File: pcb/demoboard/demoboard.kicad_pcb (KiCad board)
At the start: 2 copper layers, 68.6 x 48.3 mm, 34 parts, among them J1 BTN, J10 Conn_01x15, J11 Servo2, J12 TEMP, J13 MOT_A, J14 MOT_B, J15 CAP_T, J16 ANALOG, J17 7SEG1, J18 7SEG2, J19 STEPPER1, J2 BAT, J20 STEPPER2, J21 BITS, J22 OLED, J23 Servo3, J24 LIGHT, J3 Conn_01x15, J4 Conn_01x04, J5 Conn_01x15, J6 WSLED, J8 Conn_01x15, J9 Servo1, U2 L293D, U3 PCF8574, U4 ULN2803A

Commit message: PCB 0.1
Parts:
- removed J15: CAP_T, Connector_PinSocket_2.54mm:PinSocket_1x04_P2.54mm_Vertical
- removed J21: BITS, Connector_PinSocket_2.54mm:PinSocket_1x10_P2.54mm_Vertical
- removed REF** (x2): TestPoint_Pad_1.5x1.5mm, TestPoint:TestPoint_Pad_1.5x1.5mm
- removed U3: PCF8574, Package_DIP:DIP-16_W7.62mm
- added R5: 4K7, Resistor_THT:R_Axial_DIN0207_L6.3mm_D2.5mm_P10.16mm_Horizontal, F.Cu at (83.8, 99.7)
- added U1: 74HC595, Package_DIP:DIP-16_W7.62mm, F.Cu at (96.5, 115.6)
- J1: footprint Connector_PinSocket_2.54mm:PinSocket_1x03_P2.54mm_Vertical -> Connector_PinSocket_2.54mm:PinSocket_1x03_P2.54mm_Horizontal
- J10, J3, J5, J8: footprint Connector_PinSocket_2.54mm:PinSocket_1x15_P2.54mm_Vertical -> plain:PlainPinSocket_1x15_P2.54mm_Vertical
- J11, J23, J6, J9: footprint Connector_PinHeader_2.54mm:PinHeader_1x03_P2.54mm_Vertical -> plain:PlainPinHeader_1x03_P2.54mm_Vertical
- J12, RV1: footprint Connector_PinSocket_2.54mm:PinSocket_1x03_P2.54mm_Vertical -> plain:PlainPinSocket_1x03_P2.54mm_Vertical
- J17, J18: footprint Connector_PinSocket_2.54mm:PinSocket_1x05_P2.54mm_Vertical -> plain:PlainPinSocket_1x05_P2.54mm_Vertical
- J22: footprint Connector_PinSocket_2.54mm:PinSocket_1x04_P2.54mm_Vertical -> plain:PlainPinSocket_1x04_P2.54mm_Vertical
- J24: value LIGHT -> RV2; footprint Connector_PinSocket_2.54mm:PinSocket_1x02_P2.54mm_Vertical -> plain:PlainPinSocket_1x02_P2.54mm_Vertical
- R2, R3: value 4K7 -> 220R; footprint Resistor_THT:R_Axial_DIN0207_L6.3mm_D2.5mm_P10.16mm_Horizontal -> Resistor_THT:R_Axial_DIN0207_L6.3mm_D2.5mm_P2.54mm_Vertical
- moved R3 57.7 mm to (118.7, 90.8), turned to 180 degrees
- moved J6 49.5 mm to (120.7, 76.2), turned to 0 degrees
- moved J14 47.6 mm to (69.3, 77.5)
- moved R2 46.1 mm to (118.7, 87.0), turned to 180 degrees
- moved J1 45.7 mm to (106.7, 78.1), turned to 270 degrees
- moved J19 33.2 mm to (129.5, 118.1), turned to 180 degrees
- moved J9 22.2 mm to (127.6, 85.1), turned to 270 degrees
- moved J16 18.9 mm to (110.5, 95.2), turned to 180 degrees
- moved R1 17.6 mm to (67.3, 111.8)
- moved J18 16.9 mm to (110.5, 116.8), turned to 180 degrees
- moved U4 16.1 mm to (121.9, 116.8), turned to 180 degrees
- moved J24 13.9 mm to (71.1, 89.5)
- moved J11 13.6 mm to (127.6, 87.6), turned to 270 degrees
- moved J20 13.5 mm to (129.5, 104.1), turned to 180 degrees
- moved J4 13.5 mm to (88.9, 118.7)
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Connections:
- J10 pad 11: /D35 -> /BTN
- J13 pad 1: /MA1Y -> /MA2Y
- J13 pad 2: /MA2Y -> /MA1Y
- J14 pad 1: /MB1Y -> /MB2Y
- J14 pad 2: /MB2Y -> /MB1Y
- J17 pad 1: /B0 -> /B2
- J17 pad 2: /B1 -> /B6
- J17 pad 3: /B2 -> /B4
- J17 pad 5: /B4 -> /B7
- J18 pad 1: /B5 -> /B0
- J18 pad 2: /B6 -> /B1
- J18 pad 3: /D14 -> Net-(J18-Pad3)
- J18 pad 4: /D25 -> Net-(J18-Pad4)
- J18 pad 5: /B7 -> /B5
- J3 pad 10: /BTN -> /D19
- J3 pad 15: /BUZZ -> /D23
- J3 pad 9: /D18 -> /CLK
- J4 pad 1: /BUZZ -> /D2
- J4 pad 2: (no net) -> /D34
- J4 pad 3: /INT -> /BTN
- J5 pad 10: /BTN -> /D19
- J5 pad 15: /BUZZ -> /D23
- J5 pad 9: /D18 -> /CLK
- J6 pad 2: /D5 -> /D32
- J8 pad 11: /D35 -> /BTN
- R2 pad 1: /D22 -> /D14
- R2 pad 2: VCC -> Net-(J18-Pad4)
- R3 pad 1: /D21 -> /D25
- R3 pad 2: VCC -> Net-(J18-Pad3)
- U2 pad 15: /D18 -> /D5
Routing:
- net GND: track 25.8 -> 91.7 mm, vias 22 -> 17
- net /D2: track 2.54 -> 53.6 mm
- net /VIN: track 73.7 -> 27.6 mm
- net /BTN: track 9.72 -> 54.4 mm, vias 0 -> 2
- net VDC: track 64.4 -> 100.9 mm
- net /D25: track 53.8 -> 26.2 mm, vias 1 -> 0
- net /D36: track 50.9 -> 23.8 mm
- net /D35: track 26.7 -> 0.00 mm
- net /D21: track 39.9 -> 14.8 mm
- net Net-(J18-Pad4): track 0.00 -> 24.6 mm
- net /B5: track 51.7 -> 27.2 mm
- net /B7: track 58.5 -> 35.1 mm
- net Net-(J18-Pad3): track 0.00 -> 23.3 mm
- net /MB2Y: track 48.2 -> 25.0 mm
- net /D32: track 24.7 -> 44.6 mm
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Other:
- board size 68.6 x 48.3 mm -> 66 x 45.7 mm
- board text added: "+"
- board text added: "-"
- board text added: "1"
- board text added: "13"
- board text added: "14"
- board text added: "2"
- board text added: "25"
- board text added: "3"
- board text added: "36"
- board text added: "39"
- board text added: "3V"
- board text added: "3V3"
- board text added: "4"
- board text added: "5"
- board text added: "6"
- board text added: "7"
- board text added: "7SEG DISP"
- board text added: "A1Y"
- board text added: "A2Y"
- board text added: "B0"
- board text added: "B1"
- board text added: "B1Y"
- board text added: "B2"
- board text added: "B2Y"
- board text added: "B3"
- board text added: "B4"
- board text added: "B5"
- board text added: "B6"
- board text added: "B7"
- board text added: "BUZZ"
- board text added: "D"
- board text added: "D02"
- board text added: "D1"
- board text added: "D12"
- board text added: "D13"
- board text added: "D14"
- board text added: "D15"
- board text added: "D16"
- board text added: "D17"
- board text added: "D18"
- board text added: "D19"
- board text added: "D2"
- board text added: "D21"
- board text added: "D22"
- board text added: "D23"
- board text added: "D25"
- board text added: "D26"
- board text added: "D27"
- board text added: "D3"
- board text added: "D32"
- board text added: "D33"
- board text added: "D34"
- board text added: "D35"
- board text added: "D36"
- board text added: "D39"
- board text added: "D4"
- board text added: "D5"
- board text added: "DS18B20"
- board text added: "EN"
- board text added: "G"
- board text added: "GND"
- board text added: "I²C DISP"
- board text added: "LED"
- board text added: "MOTOR A"
- board text added: "MOTOR B"
- board text added: "NC"
- board text added: "OE"
- board text added: "P0"
- board text added: "P1"
- board text added: "P2"
- board text added: "P3"
- board text added: "P4"
- board text added: "P5"
- board text added: "P6"
- board text added: "P7"
- board text added: "RCL"
- board text added: "SCK"
- board text added: "SCL"
- board text added: "SDA"
- board text added: "SER"
- board text added: "SRCLR"
- board text added: "STEPPER 2"
- board text added: "VDC"
- board text added: "VIN"
- board text added: "WS"
- board text added: "X"
- board text added: "Y"
- board text added: "a"
- board text added: "b"
- board text added: "c"
- board text added: "d"
- board text added: "d1"
- board text added: "d2"
- board text added: "demoboard v0.1"
- board text added: "e"
- board text added: "f"
- board text added: "g"
- board text added: "hi"
- board text added: "p"

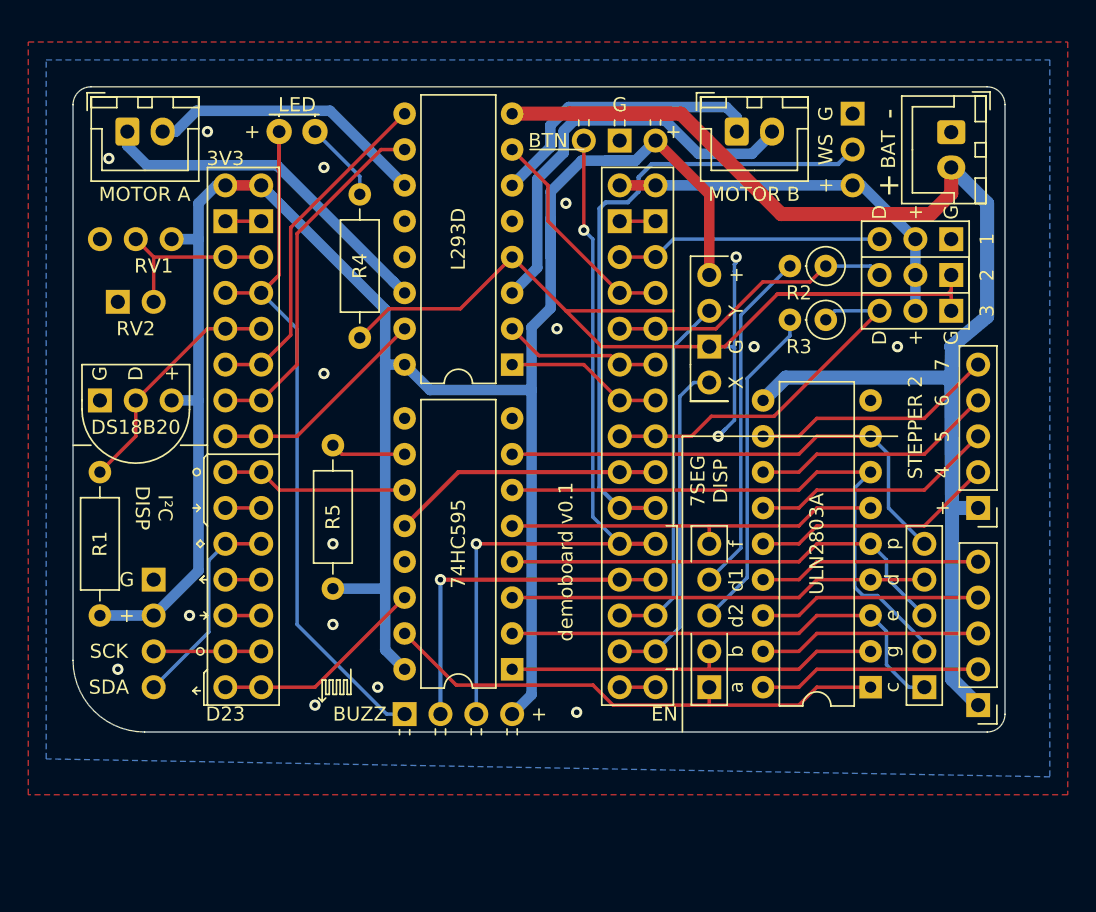
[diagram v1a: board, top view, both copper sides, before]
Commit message: Rearrange the PCB components a bit
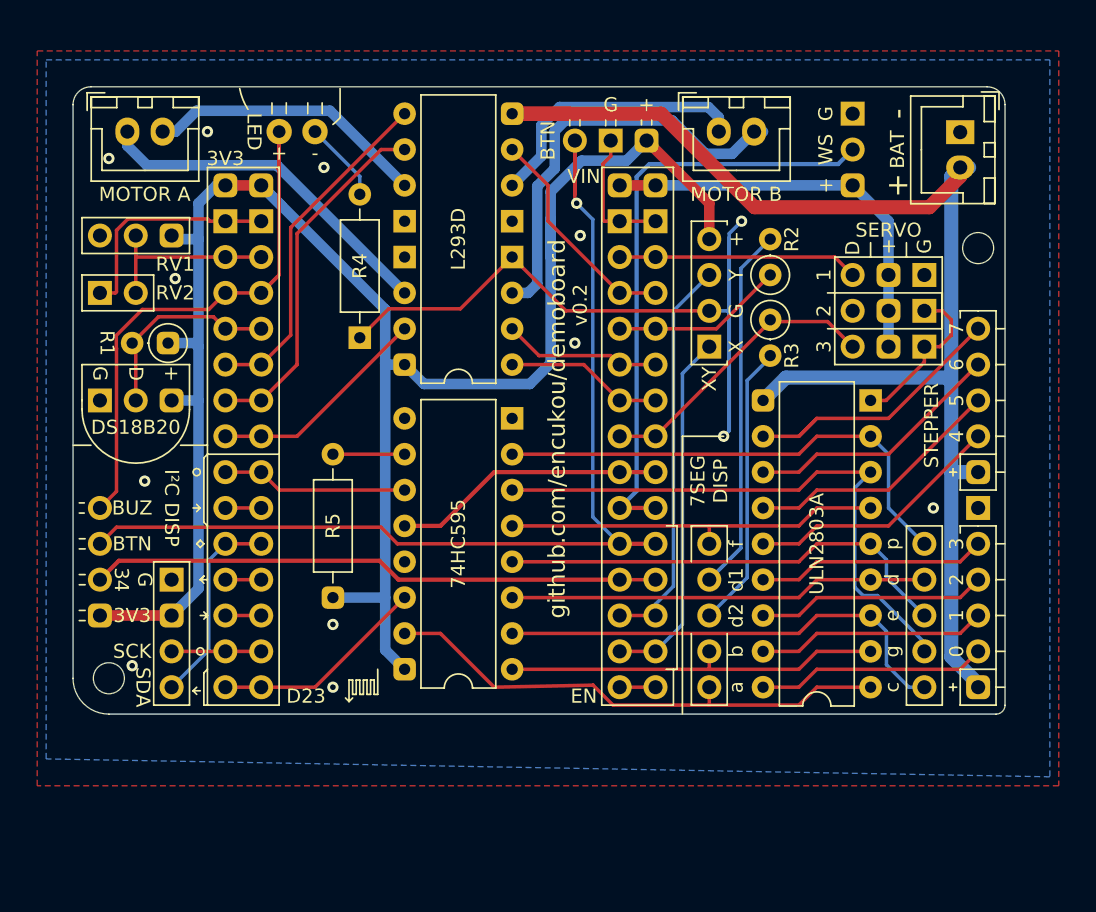
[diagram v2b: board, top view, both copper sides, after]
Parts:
- added REF**: Pad, Connector_Wire:SolderWirePad_1x01_Drill0.8mm, F.Cu at (129.5, 104.1)
- added REF**: MountingHole_2.2mm_M2, MountingHole:MountingHole_2.2mm_M2, F.Cu at (129.5, 85.7)
- added REF**: MountingHole_2.2mm_M2, MountingHole:MountingHole_2.2mm_M2, F.Cu at (67.9, 116.2)
- J16: footprint Connector_PinHeader_2.54mm:PinHeader_1x04_P2.54mm_Vertical -> plain:PlainPinSocket_1x04_P2.54mm_Vertical
- J19, J20: footprint Connector_PinHeader_2.54mm:PinHeader_1x05_P2.54mm_Vertical -> plain:PlainPinHeader_1x05_P2.54mm_Horizontal
- J24: value RV2 -> LIGHT
- R1: footprint Resistor_THT:R_Axial_DIN0207_L6.3mm_D2.5mm_P10.16mm_Horizontal -> Resistor_THT:R_Axial_DIN0207_L6.3mm_D2.5mm_P2.54mm_Vertical
- R4: value 100R -> 220R
- moved J4 26.1 mm to (67.3, 104.1), turned to 0 degrees
- moved R1 19.9 mm to (72.1, 92.5), turned to 180 degrees
- moved J20 12.7 mm to (129.5, 91.4), turned to 0 degrees
- moved J19 11.4 mm to (129.5, 106.7), turned to 0 degrees
- moved R2 3.99 mm to (114.8, 87.6), turned to 90 degrees
- moved R3 3.94 mm to (114.8, 90.8), turned to 270 degrees
- moved J11 3.18 mm to (125.7, 90.2)
- moved J23 3.17 mm to (125.7, 92.7)
- moved J9 3.17 mm to (125.7, 87.6)
- moved J16 2.54 mm to (110.5, 92.7)
- moved J24 1.42 mm to (69.8, 88.9)
- moved J13 1.27 mm to (111.2, 77.5)
- moved J22 1.27 mm to (72.4, 109.2)
- moved J1 0.64 mm to (106.0, 78.1)
- moved J2 0.64 mm to (128.3, 77.5)
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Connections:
- J19 pad 1: VDC -> Net-(J19-Pad1)
- J19 pad 5: Net-(J19-Pad5) -> VDC
- J20 pad 1: VDC -> Net-(J20-Pad1)
- J20 pad 5: Net-(J20-Pad5) -> VDC
- J4 pad 2: /D34 -> /BTN
- J4 pad 3: /BTN -> /D34
- U4 pad 11: Net-(J20-Pad5) -> Net-(J20-Pad1)
- U4 pad 12: Net-(J20-Pad4) -> Net-(J20-Pad2)
- U4 pad 14: Net-(J20-Pad2) -> Net-(J20-Pad4)
- U4 pad 15: Net-(J19-Pad5) -> Net-(J19-Pad1)
- U4 pad 16: Net-(J19-Pad4) -> Net-(J19-Pad2)
- U4 pad 18: Net-(J19-Pad2) -> Net-(J19-Pad4)
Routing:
- net VCC: track 161.5 -> 135.3 mm
- net Net-(J20-Pad1): track 0.00 -> 20.0 mm
- net /BTN: track 54.4 -> 74.0 mm, vias 2 -> 1
- net Net-(J20-Pad5): track 17.3 -> 0.00 mm
- net Net-(J19-Pad1): track 0.00 -> 16.3 mm
- net Net-(J19-Pad5): track 15.8 -> 0.00 mm
- net /D34: track 24.8 -> 40.5 mm, vias 1 -> 0
- net /D2: track 53.6 -> 40.5 mm
- net /D14: track 20.5 -> 12.5 mm
- net VDC: track 100.9 -> 94.7 mm
- net /D25: track 26.2 -> 20.6 mm
- net GND: track 91.7 -> 97.0 mm, vias 17 -> 13
- net Net-(J18-Pad4): track 24.6 -> 29.1 mm
- net Net-(J18-Pad3): track 23.3 -> 20.1 mm
- net /D4: track 17.1 -> 14.4 mm
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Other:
- board size 66 x 45.7 mm -> 66 x 44.5 mm
- board text added: "0"
- board text added: "34"
- board text added: "35"
- board text added: "BTN"
- board text added: "BUZ"
- board text added: "R1"
- board text added: "RV2"
- board text added: "SERVO"
- board text added: "STEPPER"
- board text added: "XY"
- board text added: "github.com/encukou/demoboard"
- board text added: "v0.2"
- board text removed: "BUZZ"
- board text removed: "D02"
- board text removed: "STEPPER 2"
- board text removed: "demoboard v0.1"

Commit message: PCB v0.2
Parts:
- added J7: JMP, Connector_PinHeader_2.54mm:PinHeader_1x02_P2.54mm_Vertical, F.Cu at (71.8, 90.2)
- moved J12 5.24 mm to (72.4, 97.8), turned to 270 degrees
- moved J24 2.84 mm to (67.3, 87.6), turned to 0 degrees
- moved R1 1.55 mm to (72.4, 94.0)
- moved RV1 1.02 mm to (72.4, 83.8)
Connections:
- J11 pad 3: /D14 -> /D13
- J17 pad 2: /B6 -> /B7
- J17 pad 5: /B7 -> /B6
- J19 pad 1: Net-(J19-Pad1) -> VDC
- J19 pad 5: VDC -> Net-(J19-Pad5)
- J20 pad 1: Net-(J20-Pad1) -> VDC
- J20 pad 5: VDC -> Net-(J20-Pad5)
- J23 pad 3: /D25 -> /D5
- J24 pad 1: /D15 -> /D34
- J4 pad 2: /BTN -> /D33
- J4 pad 3: /D34 -> /BTN
- J6 pad 2: /D32 -> /D25
- J9 pad 3: /D13 -> /D14
- R2 pad 1: /D14 -> /D13
- R2 pad 2: Net-(J18-Pad4) -> Net-(J18-Pad3)
- R3 pad 1: /D25 -> /D5
- R3 pad 2: Net-(J18-Pad3) -> Net-(J18-Pad4)
- RV1 pad 2: /D15 -> /D34
- RV1 pad 3: (no net) -> /RP
- U1 pad 12: /D33 -> /D32
- U2 pad 10: /D17 -> /D16
- U2 pad 15: /D5 -> /D17
- U2 pad 9: /D16 -> /D15
- U4 pad 11: Net-(J20-Pad1) -> Net-(J20-Pad2)
- U4 pad 12: Net-(J20-Pad2) -> Net-(J20-Pad3)
- U4 pad 13: Net-(J20-Pad3) -> Net-(J20-Pad4)
- U4 pad 14: Net-(J20-Pad4) -> Net-(J20-Pad5)
- U4 pad 15: Net-(J19-Pad1) -> Net-(J19-Pad2)
- U4 pad 16: Net-(J19-Pad2) -> Net-(J19-Pad3)
- U4 pad 17: Net-(J19-Pad3) -> Net-(J19-Pad4)
- U4 pad 18: Net-(J19-Pad4) -> Net-(J19-Pad5)
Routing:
- net /D5: track 15.9 -> 48.7 mm
- net /D34: track 40.5 -> 68.9 mm
- net /D32: track 42.6 -> 18.3 mm
- net /D33: track 19.4 -> 41.4 mm
- net Net-(J20-Pad1): track 20.0 -> 0.00 mm
- net Net-(J20-Pad5): track 0.00 -> 17.3 mm
- net /D25: track 20.6 -> 37.4 mm
- net Net-(J19-Pad5): track 0.00 -> 16.3 mm
- net Net-(J19-Pad1): track 16.3 -> 0.00 mm
- net /D17: track 25.5 -> 14.8 mm
- net VDC: track 94.7 -> 84.8 mm
- net Net-(J18-Pad3): track 20.1 -> 29.4 mm
- net /B6: track 41.7 -> 32.6 mm
- net /B7: track 35.1 -> 43.7 mm
- net Net-(J18-Pad4): track 29.1 -> 20.8 mm
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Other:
- board text added: "J7"
- board text added: "RP"
- board text added: "S0"
- board text added: "S1"
- board text added: "S2"
- board text added: "TCH"
- board text removed: "25"
- board text removed: "34"
- board text removed: "BTN"
- board text removed: "D"
- board text removed: "DS18B20"
- board text removed: "R1"
